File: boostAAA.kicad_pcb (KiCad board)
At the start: 2 copper layers, 70 x 14 mm, 11 parts, among them SW1 EN, U1 MCP1642B-50I/MS

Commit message: Various final tweaks
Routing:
- net (no net): vias 0 -> 20
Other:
- outline, holes or cut-outs redrawn
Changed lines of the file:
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@@
     )
   )
+  (gr_line (start 54.5 75) (end 55.5 75) (layer "B.SilkS") (width 0.15))
+  (gr_line (start 55 74.5) (end 55 75.5) (layer "B.SilkS") (width 0.15))
   (gr_line (start 105 80) (end 101.5 80) (layer "Edge.Cuts") (width 0.1))
   (gr_line (start 45 70) (end 48.5 70) (layer "Edge.Cuts") (width 0.1))
-  (gr_line (start 75 68) (end 100.5 68) (layer "Edge.Cuts") (width 0.1))
-  (gr_line (start 100.5 68) (end 100.5 69) (layer "Edge.Cuts") (width 0.1))
+  (gr_line (start 75 68) (end 99.5 68) (layer "Edge.Cuts") (width 0.1))
   (gr_line (start 101.5 70) (end 105 70) (layer "Edge.Cuts") (width 0.1))
   (gr_arc (start 49.5 69) (mid 49.207107 69.707107) (end 48.5 70) (layer "Edge.Cuts") (width 0.1))
-  (gr_line (start 75 82) (end 49.5 82) (layer "Edge.Cuts") (width 0.1))
+  (gr_line (start 75 82) (end 50.5 82) (layer "Edge.Cuts") (width 0.1))
   (gr_arc (start 101.5 70) (mid 100.792893 69.707107) (end 100.5 69) (layer "Edge.Cuts") (width 0.1))
   (gr_arc (start 100.5 81) (mid 100.792893 80.292893) (end 101.5 80) (layer "Edge.Cuts") (width 0.1))
   (gr_line (start 48.5 80) (end 45 80) (layer "Edge.Cuts") (width 0.1))
-  (gr_line (start 49.5 68) (end 75 68) (layer "Edge.Cuts") (width 0.1))
+  (gr_arc (start 50.5 82) (mid 49.792893 81.707107) (end 49.5 81) (layer "Edge.Cuts") (width 0.1))
+  (gr_line (start 50.5 68) (end 75 68) (layer "Edge.Cuts") (width 0.1))
   (gr_arc (start 105 70) (mid 110 75) (end 105 80) (layer "Edge.Cuts") (width 0.1))
   (gr_arc (start 48.5 80) (mid 49.207107 80.292893) (end 49.5 81) (layer "Edge.Cuts") (width 0.1))
-  (gr_line (start 100.5 82) (end 100.5 81) (layer "Edge.Cuts") (width 0.1))
-  (gr_line (start 49.5 68) (end 49.5 69) (layer "Edge.Cuts") (width 0.1))
-  (gr_line (start 100.5 82) (end 75 82) (layer "Edge.Cuts") (width 0.1))
-  (gr_line (start 49.5 82) (end 49.5 81) (layer "Edge.Cuts") (width 0.1))
+  (gr_arc (start 99.5 68) (mid 100.207107 68.292893) (end 100.5 69) (layer "Edge.Cuts") (width 0.1))
+  (gr_arc (start 100.5 81) (mid 100.207107 81.707107) (end 99.5 82) (layer "Edge.Cuts") (width 0.1))
+  (gr_line (start 99.5 82) (end 75 82) (layer "Edge.Cuts") (width 0.1))
   (gr_arc (start 45 80) (mid 40 75) (end 45 70) (layer "Edge.Cuts") (width 0.1))
-  (gr_text "ghub:HarkonenBade/boostAAA\n2022-04-15\nrev 1" (at 75 75) (layer "B.SilkS")
+  (gr_arc (start 49.5 69) (mid 49.792893 68.292893) (end 50.5 68) (layer "Edge.Cuts") (width 0.1))
+  (gr_text "ghub:HarkonenBade/boostAAA\n2022-04-15\nrev 1" (at 75 74) (layer "B.SilkS")
     (effects (font (size 1 1) (thickness 0.15)) (justify mirror))
   )
@@
     (effects (font (size 1 1) (thickness 0.15)))
   )
+  (via (at 101 79.5) (size 0.8) (drill 0.4) (layers "F.Cu" "B.Cu") (free) (net 0))
+  (via (at 49 70.5) (size 0.8) (drill 0.4) (layers "F.Cu" "B.Cu") (free) (net 0))
+  (via (at 49 71.5) (size 0.8) (drill 0.4) (layers "F.Cu" "B.Cu") (free) (net 0))
+  (via (at 101 74.5) (size 0.8) (drill 0.4) (layers "F.Cu" "B.Cu") (free) (net 0))
+  (via (at 49 75.5) (size 0.8) (drill 0.4) (layers "F.Cu" "B.Cu") (free) (net 0))
+  (via (at 101 73.5) (size 0.8) (drill 0.4) (layers "F.Cu" "B.Cu") (free) (net 0))
+  (via (at 49 72.5) (size 0.8) (drill 0.4) (layers "F.Cu" "B.Cu") (free) (net 0))
+  (via (at 49 78.5) (size 0.8) (drill 0.4) (layers "F.Cu" "B.Cu") (free) (net 0))
+  (via (at 101 76.5) (size 0.8) (drill 0.4) (layers "F.Cu" "B.Cu") (free) (net 0))
+  (via (at 49 73.5) (size 0.8) (drill 0.4) (layers "F.Cu" "B.Cu") (free) (net 0))
+  (via (at 101 72.5) (size 0.8) (drill 0.4) (layers "F.Cu" "B.Cu") (free) (net 0))
+  (via (at 49 79.5) (size 0.8) (drill 0.4) (layers "F.Cu" "B.Cu") (free) (net 0))
+  (via (at 49 74.5) (size 0.8) (drill 0.4) (layers "F.Cu" "B.Cu") (free) (net 0))
+  (via (at 101 78.5) (size 0.8) (drill 0.4) (layers "F.Cu" "B.Cu") (free) (net 0))
+  (via (at 49 77.5) (size 0.8) (drill 0.4) (layers "F.Cu" "B.Cu") (free) (net 0))
+  (via (at 101 77.5) (size 0.8) (drill 0.4) (layers "F.Cu" "B.Cu") (free) (net 0))
+  (via (at 101 75.5) (size 0.8) (drill 0.4) (layers "F.Cu" "B.Cu") (free) (net 0))
+  (via (at 101 71.5) (size 0.8) (drill 0.4) (layers "F.Cu" "B.Cu") (free) (net 0))
+  (via (at 101 70.5) (size 0.8) (drill 0.4) (layers "F.Cu" "B.Cu") (free) (net 0))
+  (via (at 49 76.5) (size 0.8) (drill 0.4) (layers "F.Cu" "B.Cu") (free) (net 0))
   (segment (start 66 72) (end 66 76.4) (width 0.5) (layer "F.Cu") (net 1))
   (segment (start 67.8 78.55) (end 67.8 76.475) (width 1) (layer "F.Cu") (net 1))

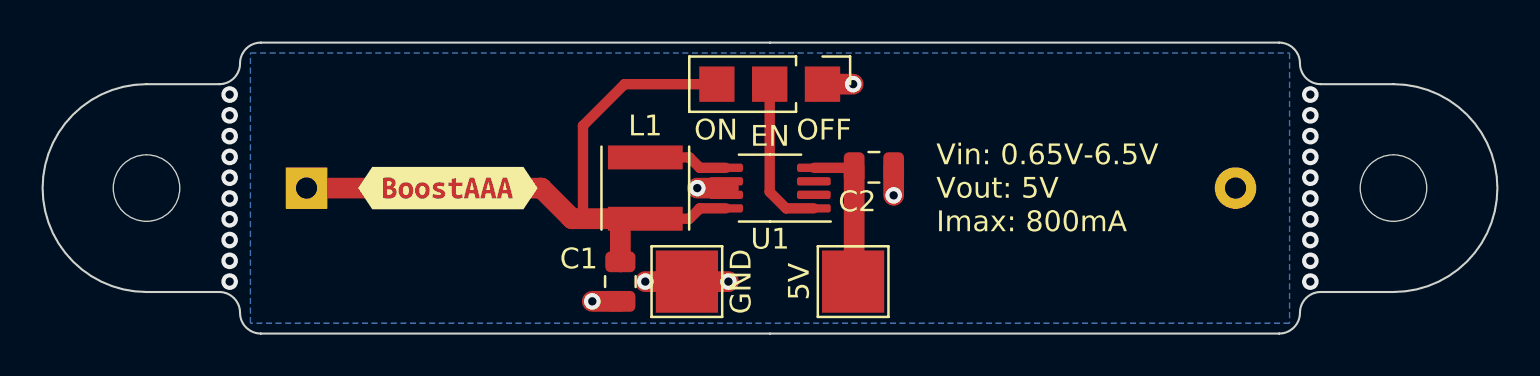
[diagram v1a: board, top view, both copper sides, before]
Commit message: Updated version to use autogen for library symbols and to allow for the use of adjustable as well as fixed versions of the regulator chip.
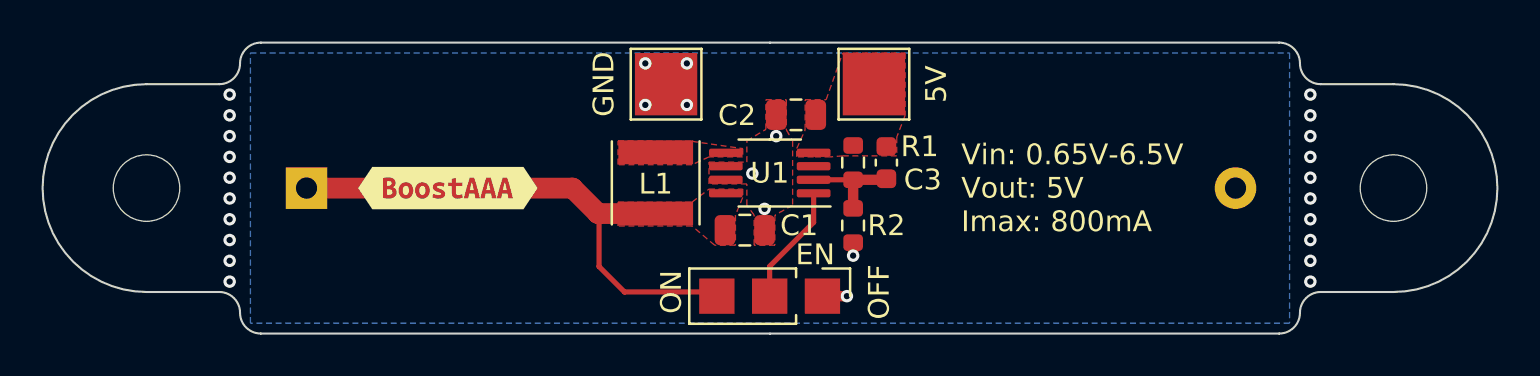
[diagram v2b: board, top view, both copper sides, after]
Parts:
- added C3: 27p, Capacitor_SMD:C_0603_1608Metric, F.Cu at (80.6, 73.8)
- added R1: 976k, Resistor_SMD:R_0603_1608Metric, F.Cu at (79.0, 73.8)
- added R2: 309k, Resistor_SMD:R_0603_1608Metric, F.Cu at (79.0, 76.8)
- moved SW1 10.2 mm to (77.5, 80.2)
- moved TP1 9.55 mm to (80.0, 70.0)
- moved TP2 9.55 mm to (70.0, 70.0)
- moved C1 6.48 mm to (73.8, 77.0), turned to 0 degrees
- moved C2 4.52 mm to (76.2, 71.5), turned to 180 degrees
- moved U1 0.73 mm to (75.0, 74.3)
- moved L1 0.56 mm to (69.5, 74.8)
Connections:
- U1 pad 2: unconnected-(U1-Pad2) -> Net-(C3-Pad2)
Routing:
- net Net-(BT1-Pad1): track 34.8 -> 26.1 mm
- net GND: track 9.67 -> 1.88 mm, vias 6 -> 9
- net +5V: track 7.47 -> 0.00 mm
- net Net-(C3-Pad2): track 0.00 -> 4.90 mm
- net Net-(L1-Pad2): track 4.09 -> 0.00 mm
- net Net-(SW1-Pad2): track 7.64 -> 5.83 mm
- added copper zone on F.Cu, net +5V
- added copper zone on F.Cu, net GND
- added copper zone on F.Cu, net Net-(BT1-Pad1)
- added copper zone on F.Cu, net Net-(L1-Pad2)
